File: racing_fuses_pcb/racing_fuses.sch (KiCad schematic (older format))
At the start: 16 parts, among them J1 Screw_Terminal_01x02, J2 Screw_Terminal_01x16, J3 Screw_Terminal_01x04, U1 Teensy3.2, U15 AXA003A0XZ, U3 SN65HVD232

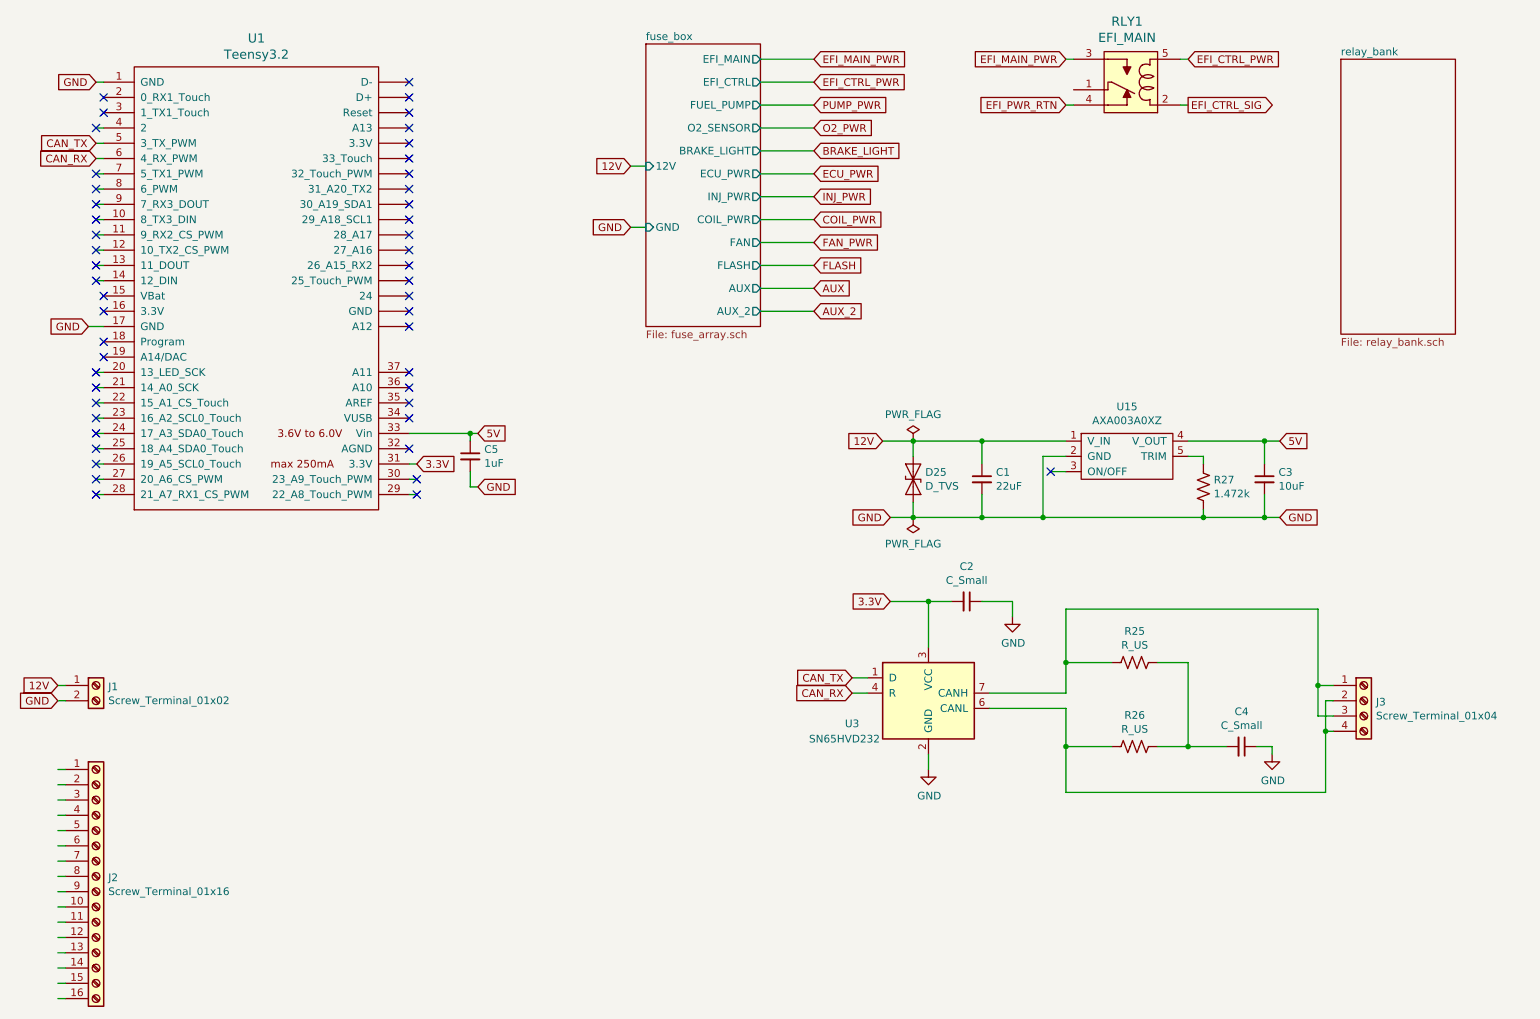
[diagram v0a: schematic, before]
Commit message: replaced relays with n-channel fets
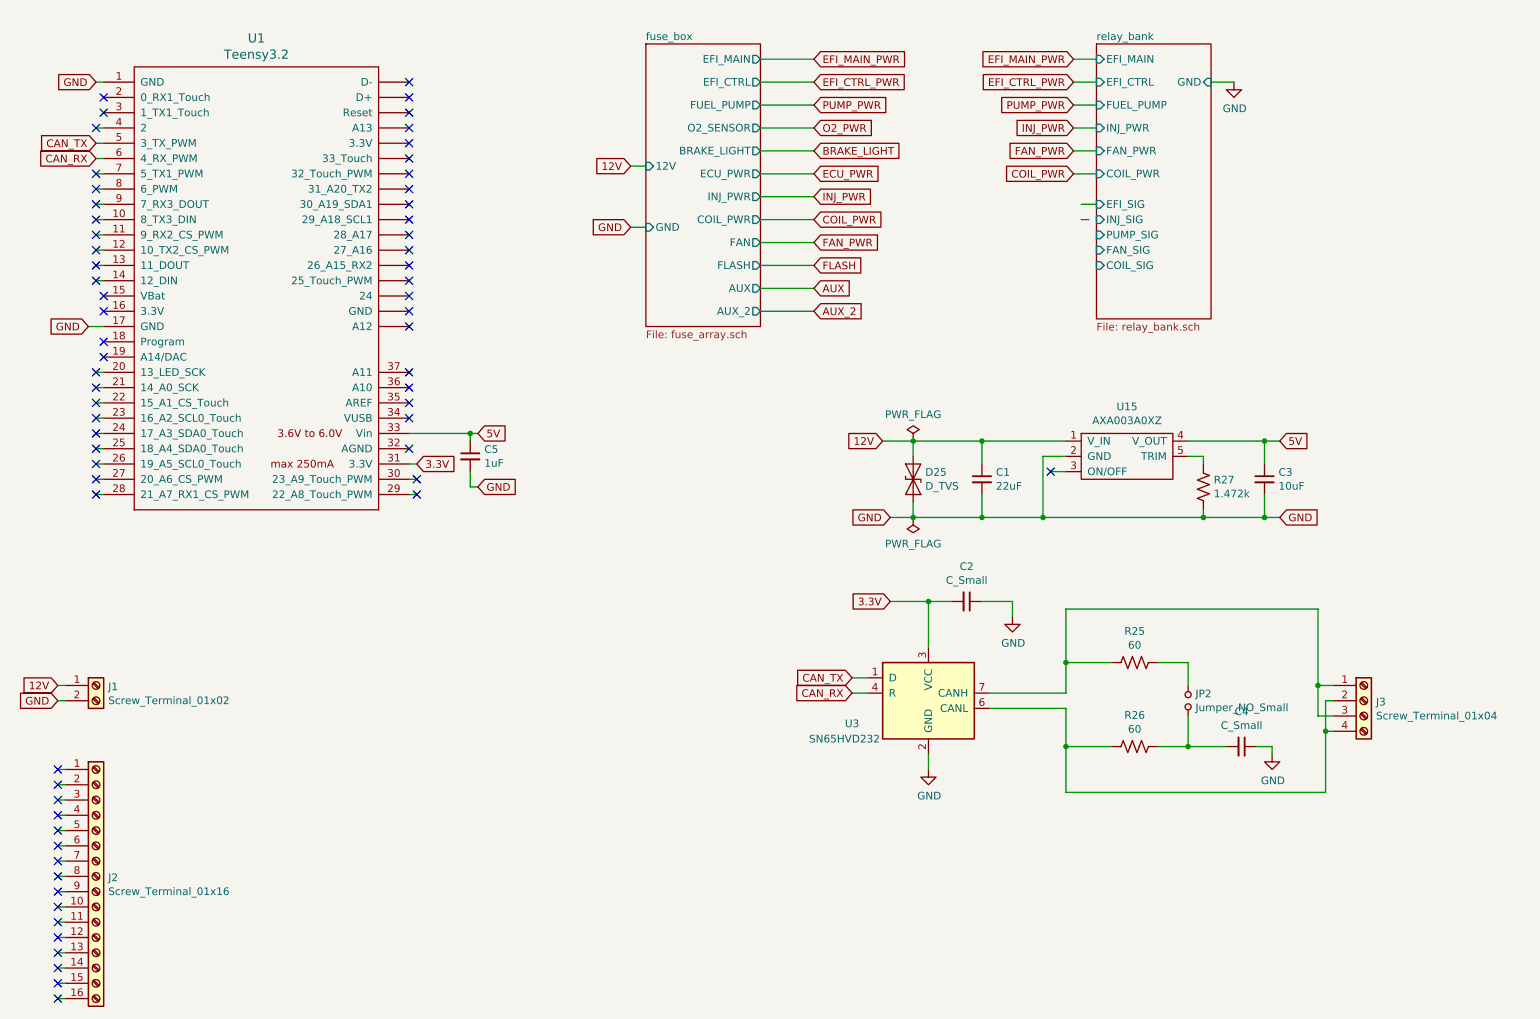
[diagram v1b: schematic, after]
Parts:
- removed RLY1: EFI_MAIN, digikey-footprints:Relay_JSM1-12V-5, symbol dk_Automotive-Relays:JSM1-12V-5
- added JP2: Jumper_NO_Small, symbol Device:Jumper_NO_Small
- R25, R26: value R_US -> 60
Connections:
- net labels removed: EFI_CTRL_SIG, EFI_PWR_RTN
- wire segments 121 -> 127
- no-connect marks 49 -> 65
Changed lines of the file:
@@
 EESchema Schematic File Version 4
+LIBS:racing_fuses-cache
 EELAYER 26 0
 EELAYER END
 $Descr A4 11693 8268
 encoding utf-8
-Sheet 1 14
+Sheet 1 20
 Title ""
 Date ""
@@
 P 8350 4850
 F 0 "R25" V 8145 4850 50  0000 C CNN
-F 1 "R_US" V 8236 4850 50  0000 C CNN
+F 1 "60" V 8236 4850 50  0000 C CNN
 F 2 "" V 8390 4840 50  0001 C CNN
 F 3 "~" H 8350 4850 50  0001 C CNN
@@
 P 8350 5400
 F 0 "R26" V 8145 5400 50  0000 C CNN
-F 1 "R_US" V 8236 5400 50  0000 C CNN
+F 1 "60" V 8236 5400 50  0000 C CNN
 F 2 "" V 8390 5390 50  0001 C CNN
 F 3 "~" H 8350 5400 50  0001 C CNN
@@
 	8500 4850 8700 4850
 Wire Wire Line
-	8700 4850 8700 5400
+	8700 4850 8700 5000
 Wire Wire Line
 	8700 5400 8500 5400
@@
 NoConn ~ 3650 3650
 NoConn ~ 3650 3750
-$Comp
-L dk_Automotive-Relays:JSM1-12V-5 RLY1
-U 1 1 5E474F26
-P 8350 1100
-F 0 "RLY1" H 8400 653 60  0000 C CNN
-F 1 "EFI_MAIN" H 8400 759 60  0000 C CNN
-F 2 "digikey-footprints:Relay_JSM1-12V-5" H 8550 1300 60  0001 L CNN
-F 3 "https://media.digikey.com/pdf/Data%20Sheets/Panasonic%20Electric%20Works%20PDFs/JS-M_Series_Rev_Dec_2011.pdf" H 8550 1400 60  0001 L CNN
-F 4 "255-1240-ND" H 8550 1500 60  0001 L CNN "Digi-Key_PN"
-F 5 "JSM1-12V-5" H 8550 1600 60  0001 L CNN "MPN"
-F 6 "Relays" H 8550 1700 60  0001 L CNN "Category"
-F 7 "Automotive Relays" H 8550 1800 60  0001 L CNN "Family"
-F 8 "https://media.digikey.com/pdf/Data%20Sheets/Panasonic%20Electric%20Works%20PDFs/JS-M_Series_Rev_Dec_2011.pdf" H 8550 1900 60  0001 L CNN "DK_Datasheet_Link"
-F 9 "/product-detail/en/panasonic-electric-works/JSM1-12V-5/255-1240-ND/274764" H 8550 2000 60  0001 L CNN "DK_Detail_Page"
-F 10 "RELAY AUTOMOTIVE SPDT 15A 12V" H 8550 2100 60  0001 L CNN "Description"
-F 11 "Panasonic Electric Works" H 8550 2200 60  0001 L CNN "Manufacturer"
-F 12 "Active" H 8550 2300 60  0001 L CNN "Status"
-	1    8350 1100
-	-1   0    0    1
-$EndComp
 Wire Wire Line
 	5900 900  6250 900
 $Sheet
-S 9700 900  750  1800
+S 8100 800  750  1800
 U 5E4970C0
 F0 "relay_bank" 50
 F1 "relay_bank.sch" 50
+F2 "EFI_MAIN" I L 8100 900 50
+F3 "EFI_CTRL" I L 8100 1050 50
+F4 "FUEL_PUMP" I L 8100 1200 50
+F5 "INJ_PWR" I L 8100 1350 50
+F6 "FAN_PWR" I L 8100 1500 50
+F7 "COIL_PWR" I L 8100 1650 50
+F8 "GND" I R 8850 1050 50
+F9 "EFI_SIG" I L 8100 1850 50
+F10 "INJ_SIG" I L 8100 1950 50
+F11 "PUMP_SIG" I L 8100 2050 50
+F12 "FAN_SIG" I L 8100 2150 50
+F13 "COIL_SIG" I L 8100 2250 50
 $EndSheet
 Text GLabel 6250 900  2    50   Input ~ 0
@@
 Text GLabel 6250 2550 2    50   Input ~ 0
 AUX_2
-Wire Wire Line
-	7950 900  7900 900
-Wire Wire Line
-	7950 1200 7900 1200
-Wire Wire Line
-	8650 900  8700 900
-Wire Wire Line
-	8650 1200 8700 1200
-Text GLabel 7900 900  0    50   Input ~ 0
+NoConn ~ 1300 5550
+NoConn ~ 1300 5650
+NoConn ~ 1300 5750
+NoConn ~ 1300 5950
+NoConn ~ 1300 5850
+NoConn ~ 1300 6050
+NoConn ~ 1300 6150
+NoConn ~ 1300 6250
+NoConn ~ 1300 6350
+NoConn ~ 1300 6450
+NoConn ~ 1300 6550
+NoConn ~ 1300 6650
+NoConn ~ 1300 6750
+NoConn ~ 1300 6850
+NoConn ~ 1300 6950
+NoConn ~ 1300 7050
+Wire Wire Line
+	8100 900  7950 900
+Wire Wire Line
+	8100 1050 7950 1050
+Wire Wire Line
+	8100 1200 7950 1200
+Wire Wire Line
+	8100 1350 7950 1350
+Wire Wire Line
+	8100 1500 7950 1500
+Wire Wire Line
+	8100 1650 7950 1650
+Wire Wire Line
+	8850 1050 9000 1050
+$Comp
+L power:GND #PWR04
+U 1 1 5E6071B9
+P 9000 1050
+F 0 "#PWR04" H 9000 800 50  0001 C CNN
+F 1 "GND" H 9005 877 50  0000 C CNN
+F 2 "" H 9000 1050 50  0001 C CNN
+F 3 "" H 9000 1050 50  0001 C CNN
+	1    9000 1050
+	1    0    0    -1
+$EndComp
+$Comp
+L Device:Jumper_NO_Small JP2
+U 1 1 5E60825F
+P 8700 5100
+F 0 "JP2" V 8654 5148 50  0000 L CNN
+F 1 "Jumper_NO_Small" V 8745 5148 50  0000 L CNN
+F 2 "" H 8700 5100 50  0001 C CNN
+F 3 "~" H 8700 5100 50  0001 C CNN
+	1    8700 5100
+	0    1    1    0
+$EndComp
+Wire Wire Line
+	8700 5200 8700 5400
+Text GLabel 7950 900  0    50   Input ~ 0
 EFI_MAIN_PWR
-Text GLabel 7900 1200 0    50   Input ~ 0
-EFI_PWR_RTN
-Text GLabel 8700 900  2    50   Input ~ 0
+Text GLabel 7950 1050 0    50   Input ~ 0
 EFI_CTRL_PWR
-Text GLabel 8700 1200 2    50   Output ~ 0
-EFI_CTRL_SIG
+Text GLabel 7950 1200 0    50   Input ~ 0
+PUMP_PWR
+Text GLabel 7950 1350 0    50   Input ~ 0
+INJ_PWR
+Text GLabel 7950 1500 0    50   Input ~ 0
+FAN_PWR
+Text GLabel 7950 1650 0    50   Input ~ 0
+COIL_PWR
+Wire Wire Line
+	8100 1850 8000 1850
+Wire Wire Line
+	8050 1950 8000 1950
 $EndSCHEMATC
